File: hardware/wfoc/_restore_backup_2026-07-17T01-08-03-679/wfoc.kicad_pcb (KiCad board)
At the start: 2 copper layers, 51 x 50 mm, 77 parts, among them Q1 NMOS, Q2 NMOS, Q3 NMOS, Q4 NMOS, Q5 NMOS, Q6 NMOS, U2 XOPA2333, U3 TSSOP20, U4 6209

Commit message: 提交最后板子修改版本
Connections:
- U1 pad 21: unconnected-(U1-GND-Pad21) -> Ia_N
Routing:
- net Ia_N: track 42.0 -> 381.5 mm, vias 126 -> 170
- net Ia_P: track 12.3 -> 20.3 mm
- net Ib_P: track 21.5 -> 27.4 mm, vias 0 -> 1
- net LO2: track 0.00 -> 5.50 mm, vias 0 -> 1
- net Net-(Q2-G): track 0.00 -> 4.92 mm
- net LO1: track 2.70 -> 4.40 mm, vias 1 -> 2
- net IC_ib: track 9.99 -> 11.6 mm
- net +BATT: track 194.6 -> 195.2 mm, vias 1 -> 18
- net unconnected-(U1-GND-Pad21): vias 1 -> 0
- net +3.3V: vias 8 -> 10
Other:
- outline, holes or cut-outs redrawn

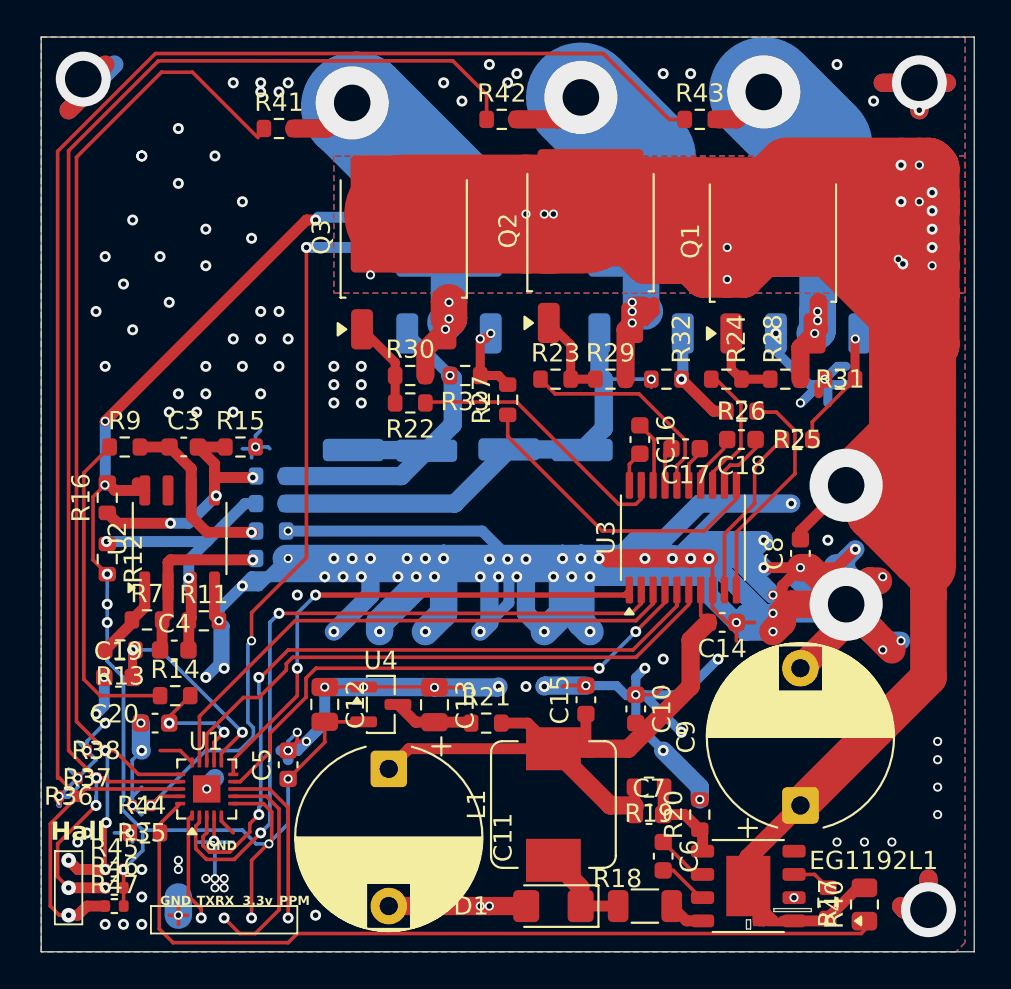
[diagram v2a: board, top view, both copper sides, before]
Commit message: 过大电流线加粗处理
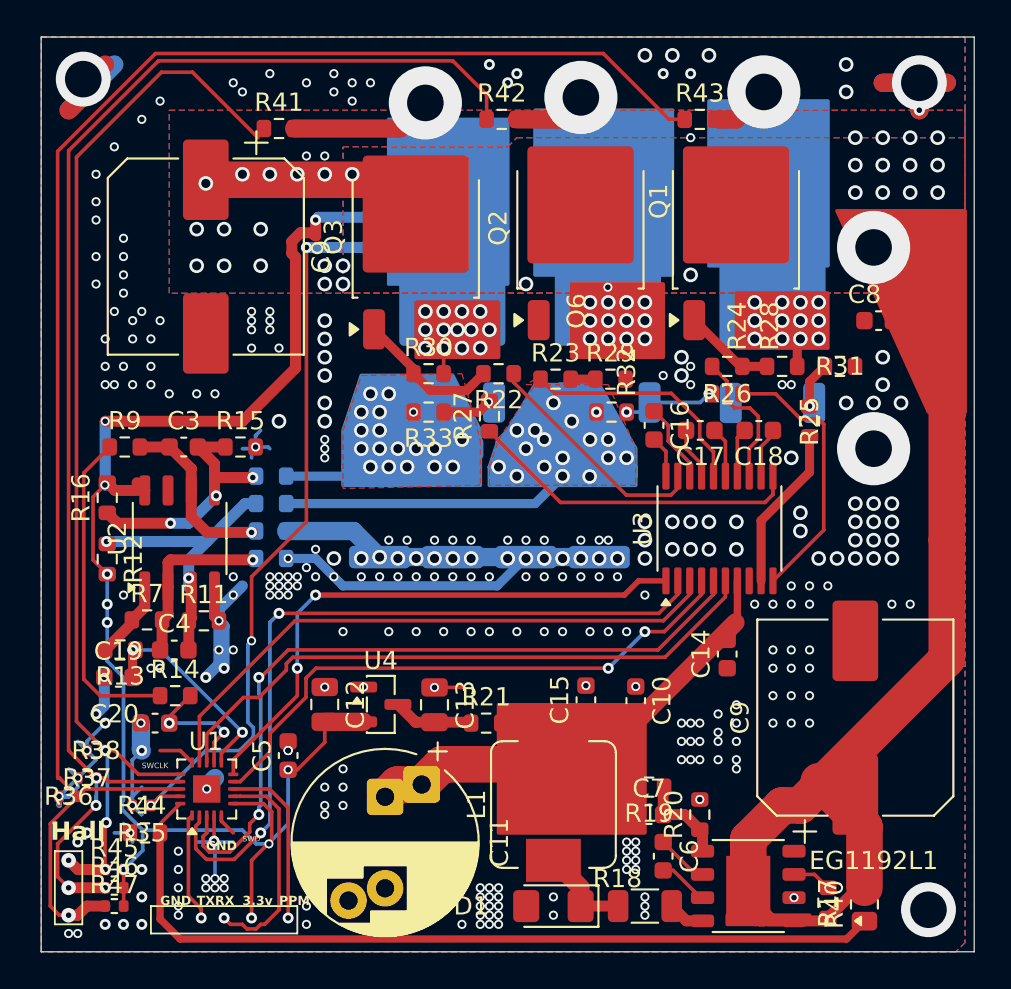
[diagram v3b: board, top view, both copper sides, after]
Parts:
- added C9: 470uf 80V, Capacitor_SMD:CP_Elec_10x12.5, F.Cu at (126.5, 75.0)
- C11: footprint Capacitor_THT:CP_Radial_D10.0mm_P7.50mm -> Capacitor_THT:CP_Radial_D10.0mm_P5.00mm_P7.50mm
- C9: footprint Capacitor_THT:CP_Radial_D10.0mm_P7.50mm -> Capacitor_SMD:CP_Elec_10x12.5
- moved C8 13.4 mm to (163.3, 78.5), turned to 0 degrees
- moved C9 5.66 mm to (162.0, 100.2)
- moved R22 5.08 mm to (142.5, 81.4)
- moved Q5 4.53 mm to (157.5, 78.0)
- moved Q6 4.19 mm to (148.5, 77.9)
- moved Q4 3.78 mm to (140.0, 77.9)
- moved R32 3.50 mm to (148.7, 83.5)
- moved R33 2.83 mm to (138.7, 83.5)
- moved Q1 2.15 mm to (155.5, 73.4)
- moved U3 2.06 mm to (154.6, 89.9)
- moved C14 1.75 mm to (155.0, 96.7), turned to 90 degrees
- moved C11 1.54 mm to (136.3, 104.5)
- moved R2 1.44 mm to (140.0, 88.5)
- moved R6 1.43 mm to (136.0, 88.5)
- moved R27 1.35 mm to (142.0, 83.7)
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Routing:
- net Ia_N: track 381.5 -> 92.0 mm, vias 170 -> 316
- net +BATT: track 195.2 -> 68.1 mm, vias 18 -> 34
- net Motor_V: track 29.2 -> 4.00 mm, vias 4 -> 14
- net Motor_W: track 22.2 -> 6.09 mm, vias 4 -> 13
- net Ia_P: track 20.3 -> 6.86 mm, vias 1 -> 18
- net Ib_P: track 27.4 -> 15.7 mm, vias 1 -> 17
- net Motor_U: track 21.1 -> 10.5 mm, vias 4 -> 14
- net +12V: track 37.1 -> 42.6 mm
- net +3.3V: track 76.4 -> 81.6 mm
- net LO3: track 6.47 -> 2.52 mm
- net Net-(Q2-G): track 4.92 -> 1.35 mm
- net Net-(Q3-G): track 4.78 -> 7.91 mm
- net Net-(U3-HO2): track 11.9 -> 14.4 mm
- net PWM_CL: track 31.8 -> 34.1 mm
- net PWM_BH: track 39.5 -> 41.7 mm
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- added copper zone on F.Cu, net Ia_P
- added copper zone on F.Cu, net Ib_P
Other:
- outline, holes or cut-outs redrawn
- board text added: "SWCLK"
- board text added: "SWD"

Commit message: 修改PCB大小和 电流采样开尔文线
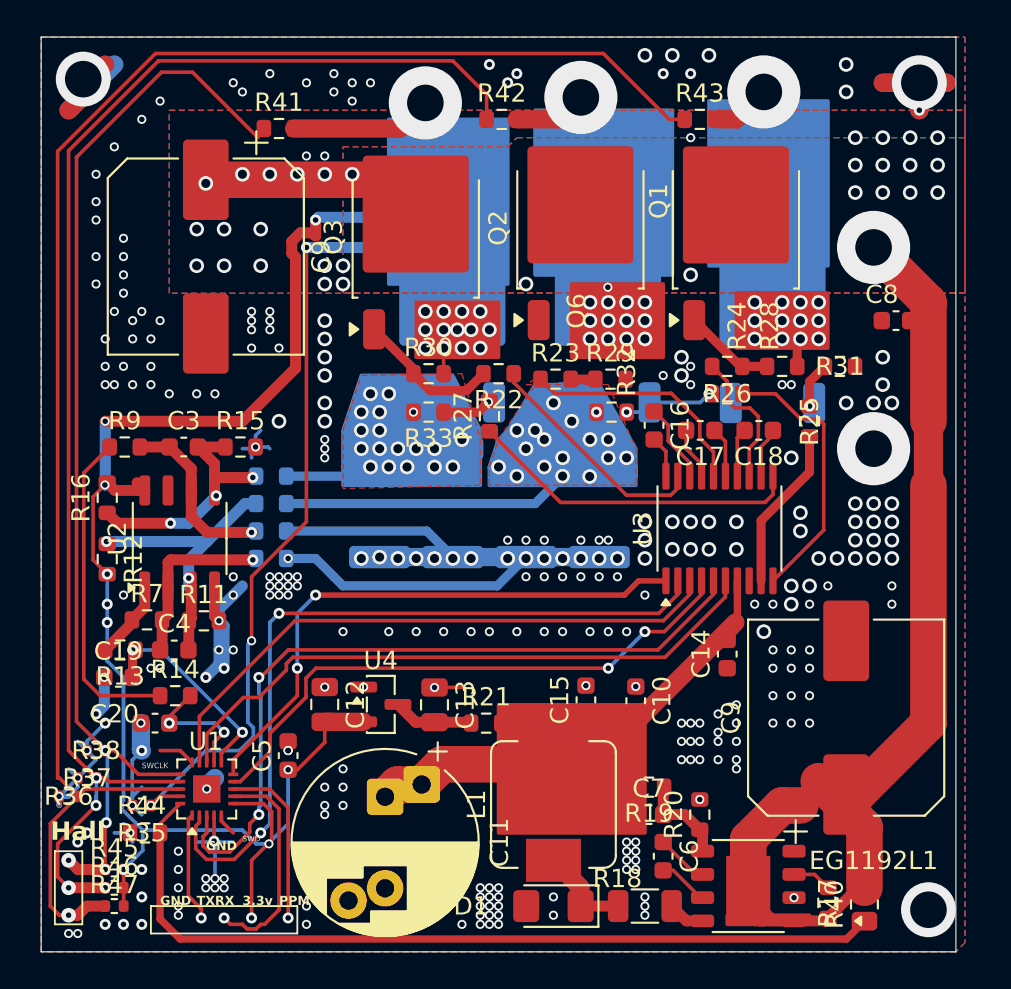
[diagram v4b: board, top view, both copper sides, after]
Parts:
- moved C8 0.95 mm to (164.2, 78.5)
- moved C9 0.50 mm to (161.5, 100.2)
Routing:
- net Ia_N: track 92.0 -> 96.0 mm, vias 316 -> 299
- net +BATT: track 68.1 -> 65.9 mm
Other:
- board size 51 x 50 mm -> 50 x 50 mm

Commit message: vesc 风格的第一个版本程序
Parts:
- added C100: 104, Resistor_SMD:R_0402_1005Metric, F.Cu at (123.5, 108.0)
- R40: footprint Resistor_SMD:R_0805_2012Metric -> Resistor_SMD:R_0603_1608Metric
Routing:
- net Net-(D1-K): track 6.92 -> 10.7 mm
- net LO3: vias 1 -> 2
- net Ia_N: vias 299 -> 301
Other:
- board text added: "Bat+"
- board text added: "Bat-"
- board text added: "MaxwellWang 2026/8/3 V1.0.2"
